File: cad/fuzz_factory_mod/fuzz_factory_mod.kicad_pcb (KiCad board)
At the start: 2 copper layers, 138 x 114 mm, 390 parts, among them J101 Conn_interface_1, J102 Conn_interface_2, J1701 Barrel_Jack_Switch, J1702 Conn_Battery, J1703 CONN_AUDIO_IN, J1704 CONN_AUDIO_OUT, J201 Conn_MCU_SWD, J2801 CONN_AUDIO_OUT_REF, J2802 CONN_EXP_1, J2803 CONN_EXP_2, J301 USB_B_Micro, J401 USB_B_Micro, J901 CONN_MIDI_IN, J902 CONN_MIDI_THRU, J903 CONN_MIDI_OUT, J904 Conn_01x10_Female, J905 Conn_01x10_Female, K2101 Fujitsu-Takamisawa-A_AL, Q1301 MMDT3904, Q1302 MMDT3904, Q1602 DTA123Y, Q1603 DTA123Y, Q1604 DTA123Y, Q1605 DTA123Y, Q1701 DTC114Y, Q1702 DTA114E, Q2201 BCP51, Q601 DTA123Y, Q602 DTA123Y, Q603 DTA123Y, Q604 DTA123Y, Q801 MMDT3904, Q802 MMDT3904, SW1101 SW_PUSH, SW1201 SW_PUSH, SW1301 SW_PUSH, U1101 LM1458, U1102 MC33202, U1201 LM2903, U1202 MC33202, U1501 LM1458, U1502 MC33202, U1503 MC33202, U1601 4050, U1602 4049, U1603 4504, U1604 MC33202, U1701 LM1458, U1702 MC33202, U1803 LM1458, U1804 MC33202, U1901 LM2903, U201 STM32F303VCTx, U2201 TL072, U2202 LM2674M-ADJ, U2203 LM78L05_SO8, U301 USBLC6-2SC6, U302 FT230XS, U401 USBLC6-2SC6, U501 74LS132, U601 4050, U602 4504, U603 MC33202, U604 4049, U701 AD5262_ABC, U901 4N25, Y201 Resonator_Small

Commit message: Continued layout.
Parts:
- moved C2211 304.2 mm to (234.6, 109.4), turned to 0 degrees
- moved C2202 284.5 mm to (225.7, 109.4)
- moved C2206 277.4 mm to (225.7, 116.0), turned to 0 degrees
- moved R1702 273.0 mm to (102.2, 49.8)
- moved C210 270.5 mm to (139.8, 90.8), turned to 0 degrees
- moved R207 267.4 mm to (136.8, 90.8), turned to 0 degrees
- moved R1505 262.2 mm to (97.8, 106.2), turned to 270 degrees
- moved D1701 257.7 mm to (79.8, 42.0)
- moved R808 254.7 mm to (104.8, 64.2), turned to 0 degrees
- moved Q1701 254.5 mm to (80.8, 46.8), turned to 180 degrees
- moved R815 254.4 mm to (104.8, 65.9), turned to 0 degrees
- moved R807 254.2 mm to (104.8, 67.7), turned to 0 degrees
- moved K2101 253.6 mm to (69.5, 46.8), turned to 0 degrees
- moved R1510 253.4 mm to (92.2, 125.5), turned to 90 degrees
- moved R1306 253.4 mm to (129.5, 104.5), turned to 0 degrees
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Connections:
- C907 pad 2: +5V -> /MCU/MIDI/+5V_IN
- R205 pad 1: +5V -> /MCU/MIDI/+5V_IN
- R206 pad 1: +5V -> /MCU/MIDI/+5V_IN
- R918 pad 2: +5V -> /MCU/MIDI/+5V_IN
- R920 pad 1: +5V -> /MCU/MIDI/+5V_IN
- R922 pad 1: +5V -> /MCU/MIDI/+5V_IN
- U501 pad 14: +5V -> /MCU/MIDI/+5V_IN
- U901 pad 6: +5V -> /MCU/MIDI/+5V_IN
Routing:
- net +3V3: track 88.2 -> 4.71 mm, vias 2 -> 0
- net BYPASS_CMD: track 0.00 -> 82.0 mm, vias 0 -> 4
- net DISP_ENABLE: track 0.00 -> 80.5 mm, vias 0 -> 2
- net SPI2_MOSI: track 0.00 -> 77.3 mm, vias 0 -> 2
- net SPI2_SCK: track 0.00 -> 76.5 mm, vias 0 -> 2
- net /CONNECTORS/AUDIO_IN_CONN: track 0.00 -> 67.2 mm
- net GNDD: track 16.9 -> 59.5 mm, vias 5 -> 16
- net ENC3_IN_CW: track 0.00 -> 34.8 mm
- net ENC3_IN_CCW: track 0.00 -> 34.7 mm
- net ENC1_IN_CCW: track 0.00 -> 34.6 mm, vias 0 -> 2
- net /CONNECTORS/AUDIO_OUT_CONN: track 0.00 -> 34.0 mm
- net DISP_LATCH: track 0.00 -> 33.3 mm, vias 0 -> 2
- net +9V: track 22.9 -> 54.0 mm
- net ENC1__LED_GREEN: track 0.00 -> 30.0 mm, vias 0 -> 2
- net ENC1_IN_CW: track 0.00 -> 28.7 mm, vias 0 -> 2
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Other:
- board text added: "0.5mm clearance with enclosure wall"

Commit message: Continued layout.
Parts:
- C1112, C701: moved to F.Cu
- moved C2211 56.5 mm to (180.8, 92.5), turned to 180 degrees
- moved C1110 56.0 mm to (135.8, 89.6)
- moved R207 48.3 mm to (166.5, 52.8), turned to 270 degrees
- moved R208 48.0 mm to (168.8, 52.8), turned to 270 degrees
- moved C2202 46.2 mm to (180.8, 98.5), turned to 180 degrees
- moved C210 44.1 mm to (166.5, 55.8), turned to 270 degrees
- moved C211 43.7 mm to (168.8, 55.8), turned to 270 degrees
- moved Q1702 36.7 mm to (171.2, 90.2)
- moved C2206 33.5 mm to (199.5, 95.0), turned to 270 degrees
- moved R2804 22.5 mm to (187.5, 49.5)
- moved R2802 19.3 mm to (166.5, 50.0)
- moved C1304 16.7 mm to (184.2, 125.0)
- moved R505 16.4 mm to (140.2, 96.5), turned to 0 degrees
- moved R804 16.3 mm to (94.8, 64.2), turned to 0 degrees
- moved R502 14.0 mm to (140.2, 98.2), turned to 0 degrees
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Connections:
- net Net-(C2207-Pad2) renamed /PSU/DCDC_VSW
- J102 pad 5: ENC2_IN_CCW -> ENC2_IN_CW
- U201 pad 82: ENC2_IN_CCW -> ENC2_IN_CW
- U201 pad 92: ENC2_IN_CCW -> (no net)
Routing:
- net AUDIO_OUT_FX: track 0.00 -> 182.0 mm, vias 0 -> 7
- net AUDIO_IN_FX: track 0.00 -> 134.1 mm, vias 0 -> 4
- net /MCU/SW_PRESET_UP: track 0.00 -> 119.3 mm, vias 0 -> 2
- net /MCU/UART5_RX: track 1.27 -> 115.8 mm, vias 0 -> 2
- net /MCU/SW_PRESET_DOWN: track 8.50 -> 116.8 mm, vias 0 -> 2
- net USB_DP: track 0.00 -> 100.6 mm, vias 0 -> 2
- net USB_DM: track 0.00 -> 100.1 mm, vias 0 -> 2
- net INPUT_CAPTURE_2: track 2.54 -> 96.7 mm, vias 0 -> 2
- net INPUT_CAPTURE_1: track 4.76 -> 93.8 mm, vias 0 -> 2
- net /ANALOG/IN_AUDIO_VCA: track 4.12 -> 84.0 mm, vias 0 -> 3
- net Net-(C2201-Pad1): track 0.00 -> 75.4 mm
- net /MCU/SW_BYPASS: track 2.30 -> 76.0 mm, vias 1 -> 5
- net Ref_Stab_DAC_PWM_MSB: track 13.2 -> 84.6 mm, vias 1 -> 4
- net Ref_Stab_DAC_PWM_LSB: track 6.32 -> 76.0 mm, vias 1 -> 5
- net VCA_IN_PWM: track 0.00 -> 68.7 mm, vias 0 -> 2
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- added copper zone on F.Cu, net +3V3
- added copper zone on F.Cu, net /PSU/DCDC_VSW

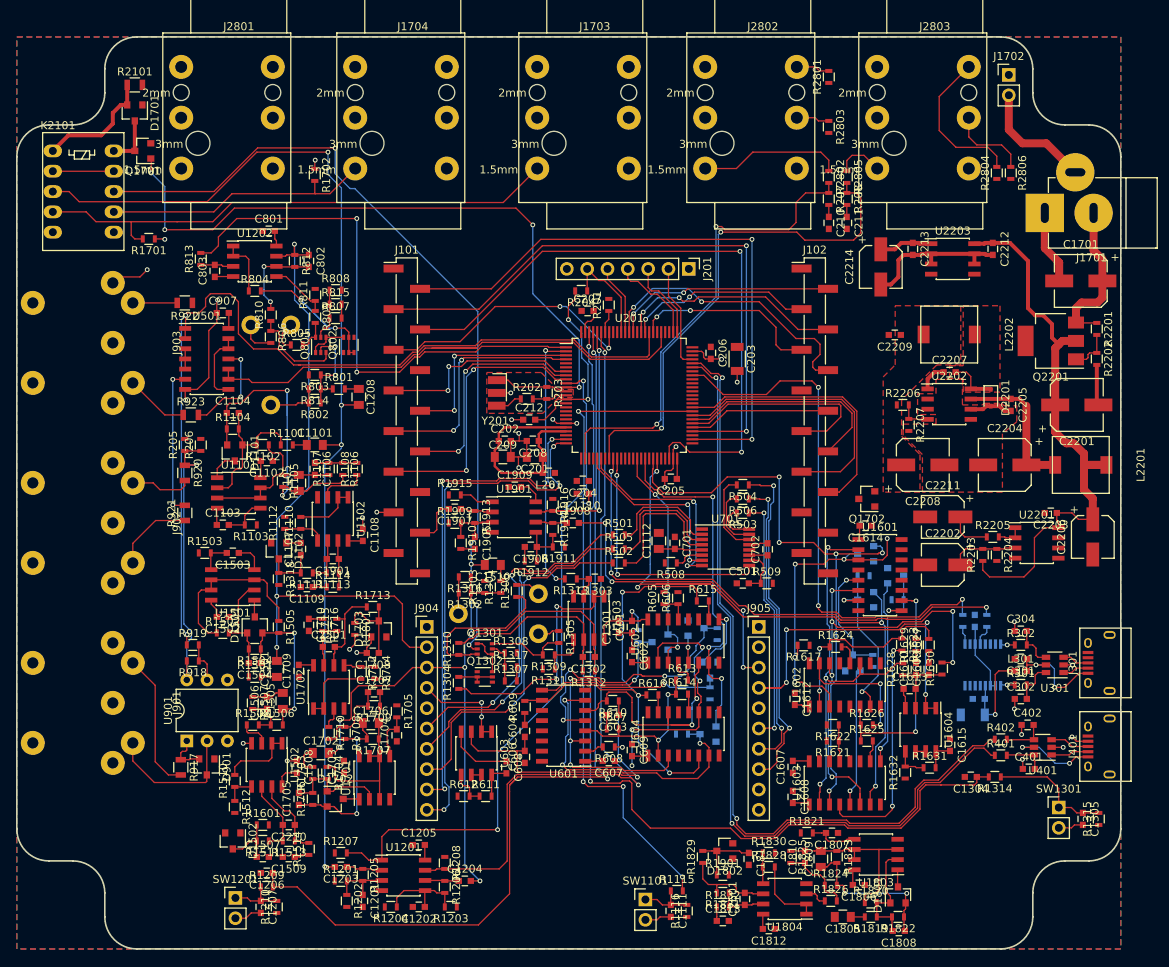
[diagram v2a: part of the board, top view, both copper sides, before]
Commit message: Continued layout. Started power planes.
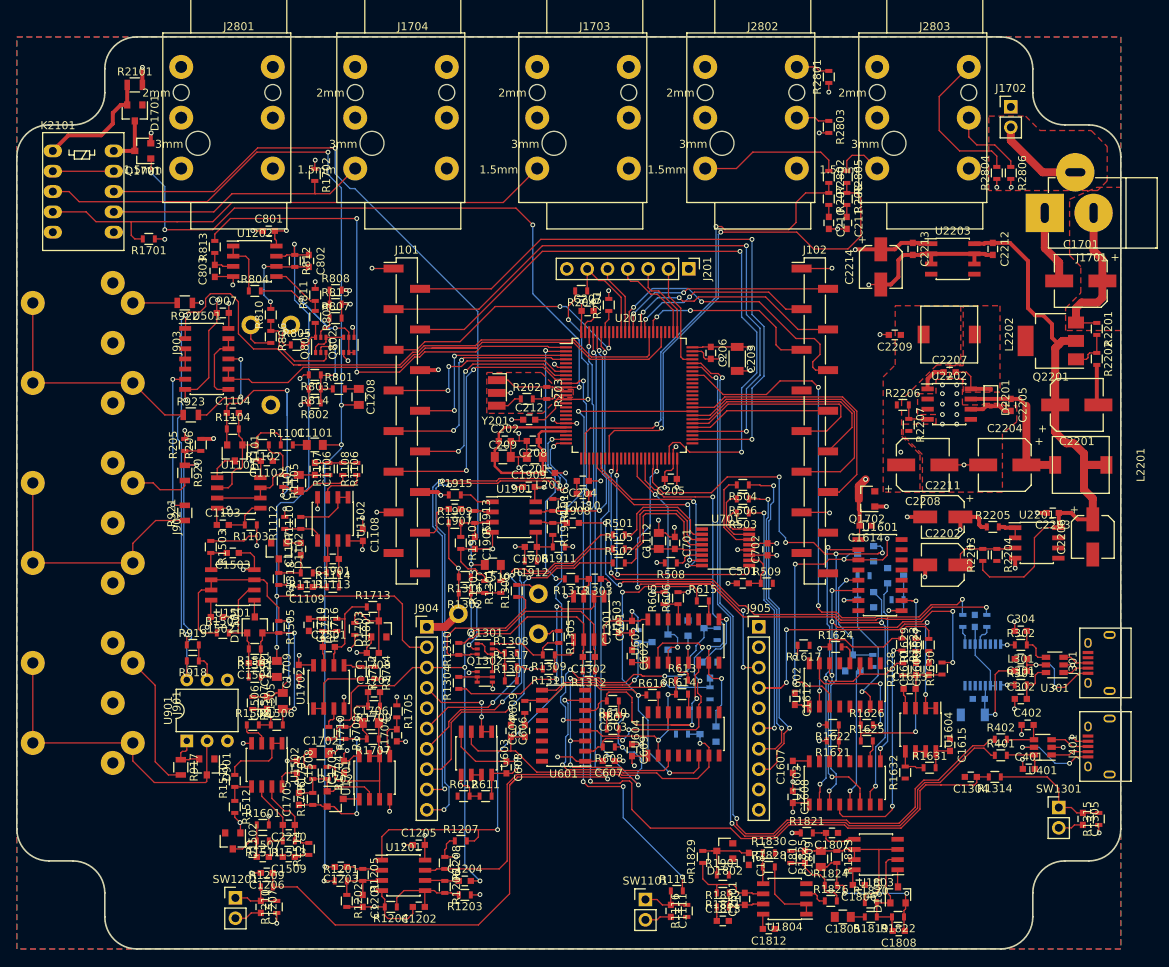
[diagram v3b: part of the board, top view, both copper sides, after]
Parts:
- moved R1207 15.1 mm to (120.5, 133.0)
- moved J1702 4.01 mm to (189.2, 41.2)
- moved C606 3.69 mm to (126.8, 119.2), turned to 270 degrees
- moved R1203 2.30 mm to (121.0, 139.8)
- moved R813 2.30 mm to (89.8, 58.8)
- moved C1909 1.75 mm to (129.0, 88.8)
- moved R2205 1.25 mm to (187.0, 93.8)
- moved R1503 1.06 mm to (89.2, 96.2), turned to 270 degrees
- moved C1502 0.75 mm to (90.0, 105.0)
- moved C2203 0.25 mm to (194.5, 92.0)
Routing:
- net +3V3: track 9.09 -> 612.9 mm, vias 0 -> 20
- net +9V: track 74.6 -> 559.0 mm, vias 2 -> 26
- net VCOM: track 5.48 -> 189.3 mm, vias 0 -> 4
- net +BATT: track 19.3 -> 161.9 mm, vias 0 -> 1
- net +5V: track 6.67 -> 117.2 mm, vias 0 -> 3
- net GNDA: track 52.5 -> 131.2 mm, vias 11 -> 53
- net /MCU/MIDI/+5V_IN: track 38.6 -> 76.8 mm, vias 1 -> 3
- net GNDD: track 92.0 -> 115.8 mm, vias 17 -> 39
- net Net-(J902-Pad5): track 10.1 -> 32.6 mm
- net Net-(J903-Pad5): track 7.96 -> 30.5 mm
- net Net-(D901-Pad3): track 17.9 -> 40.4 mm
- net Net-(C1505-Pad2): track 26.1 -> 37.0 mm, vias 0 -> 2
- net Net-(J1701-Pad3): track 14.8 -> 11.4 mm
- net ADC_FF_pol2: track 65.4 -> 68.3 mm
- net ADC_FF_pol1: track 63.1 -> 65.7 mm
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- added copper zone on In2.Cu, net +3V3
- added copper zone on F.Cu, net +BATT
- added copper zone on In2.Cu, net +BATT
- added copper zone on In1.Cu, net GNDA
- added copper zone on In2.Cu, net GNDA
- added copper zone on F.Cu, net Net-(J1701-Pad3)
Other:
- copper layers 2 -> 4

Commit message: Layout continued : finished power polys on internal layer.
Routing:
- net +3V3: track 612.9 -> 610.2 mm
- net VCOM: track 189.3 -> 187.1 mm
- net /MCU/MIDI/+5V_IN: track 76.8 -> 77.7 mm
- added copper zone on In2.Cu, net +5V
- added copper zone on In2.Cu, net +9V
- added copper zone on In2.Cu, net VCOM

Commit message: Continued layout.
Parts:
- removed NT101, NT102: Net-Tie_2, Oddities:NetTie-II
- moved R2801 8.31 mm to (168.8, 45.5)
- moved R2803 1.75 mm to (166.5, 45.5)
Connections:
- C1110 pad 2: GNDD -> GNDA
- C1111 pad 2: GNDD -> GNDA
- C1206 pad 2: GNDD -> GNDA
- C1207 pad 2: GNDD -> GNDA
- C1304 pad 2: GNDD -> GNDA
- C1305 pad 2: GNDD -> GNDA
- C1701 pad 2: GNDPWR -> GNDA
- C203 pad 2: GNDD -> GNDA
- C204 pad 2: GNDD -> GNDA
- C205 pad 2: GNDD -> GNDA
- C206 pad 2: GNDD -> GNDA
- C207 pad 2: GNDD -> GNDA
- C210 pad 2: GNDD -> GNDA
- C211 pad 2: GNDD -> GNDA
- C212 pad 1: GNDD -> GNDA
- C2201 pad 2: GNDD -> GNDA
- C2204 pad 2: GNDD -> GNDA
- C2205 pad 2: GNDD -> GNDA
- C2206 pad 2: GNDD -> GNDA
- C2208 pad 2: GNDD -> GNDA
- C2209 pad 2: GNDD -> GNDA
- C2212 pad 2: GNDD -> GNDA
- C2213 pad 2: GNDD -> GNDA
- C2214 pad 2: GNDD -> GNDA
- C301 pad 2: GNDD -> GNDA
- C302 pad 1: GNDD -> GNDA
- C303 pad 2: GNDD -> GNDA
- C304 pad 1: GNDD -> GNDA
- C305 pad 2: GNDD -> GNDA
- C306 pad 1: GNDD -> GNDA
- C401 pad 1: GNDD -> GNDA
- C402 pad 1: GNDD -> GNDA
- C702 pad 1: GNDD -> GNDA
- C907 pad 1: GNDD -> GNDA
- D2201 pad 2: GNDD -> GNDA
- J101 pad 1: GNDD -> GNDA
- J101 pad 13: GNDD -> GNDA
- J102 pad 1: GNDD -> GNDA
- J102 pad 13: GNDD -> GNDA
- J1701 pad 1: GNDPWR -> GNDA
- J1702 pad 1: GNDS -> Net-(J1702-Pad1)
- J1703 pad 1: GNDPWR -> GNDA
- J1703 pad 4: GNDPWR -> GNDA
- J1703 pad 5: (no net) -> Net-(J1702-Pad1)
- J1704 pad 1: GNDPWR -> GNDA
- J1704 pad 4: GNDPWR -> GNDA
- J1704 pad 5: GNDS -> (no net)
- J201 pad 7: GNDD -> GNDA
- J2801 pad 1: GNDPWR -> GNDA
- J2801 pad 4: GNDPWR -> GNDA
- J2802 pad 1: GNDD -> GNDA
- J2802 pad 6: GNDD -> GNDA
- J2803 pad 1: GNDD -> GNDA
- J2803 pad 6: GNDD -> GNDA
- J301 pad 4: GNDD -> GNDA
- J301 pad 5: GNDD -> GNDA
- J301 pad 6: GNDD -> GNDA
- J401 pad 4: GNDD -> GNDA
- J401 pad 5: GNDD -> GNDA
- J401 pad 6: GNDD -> GNDA
- J902 pad 2: GNDD -> GNDA
- J903 pad 2: GNDD -> GNDA
- Q1701 pad 2: GNDPWR -> GNDA
- R201 pad 2: GNDD -> GNDA
- R2202 pad 2: GNDD -> GNDA
- R2207 pad 2: GNDD -> GNDA
- R2803 pad 2: GNDD -> GNDA
- R2806 pad 2: GNDD -> GNDA
- SW1101 pad 2: GNDD -> GNDA
- SW1201 pad 2: GNDD -> GNDA
- SW1301 pad 2: GNDD -> GNDA
- U201 pad 49: GNDD -> GNDA
- U201 pad 74: GNDD -> GNDA
- U201 pad 99: GNDD -> GNDA
- U2202 pad 6: GNDD -> GNDA
- U2203 pad 2: GNDD -> GNDA
- U2203 pad 3: GNDD -> GNDA
- U2203 pad 6: GNDD -> GNDA
- U2203 pad 7: GNDD -> GNDA
- U301 pad 2: GNDD -> GNDA
- U302 pad 13: GNDD -> GNDA
- U302 pad 5: GNDD -> GNDA
- U401 pad 2: GNDD -> GNDA
- U501 pad 7: GNDD -> GNDA
- U701 pad 11: GNDD -> GNDA
- U901 pad 4: GNDD -> GNDA
- Y201 pad 2: GNDD -> GNDA
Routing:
- net GNDA: track 131.2 -> 270.8 mm, vias 53 -> 99
- net GNDD: track 115.8 -> 0.00 mm, vias 39 -> 0
- net +9V: track 559.0 -> 644.3 mm, vias 26 -> 34
- net Net-(J1702-Pad1): track 0.00 -> 68.8 mm
- net AUDIO_OUT_FX: track 182.0 -> 240.0 mm, vias 7 -> 11
- net +3V3: track 610.2 -> 626.4 mm, vias 20 -> 25
- net GNDPWR: track 10.6 -> 0.00 mm, vias 1 -> 0
- net Net-(J2802-Pad4): track 4.21 -> 13.9 mm
- net +BATT: track 161.9 -> 158.3 mm
- net /MCU/SW_BYPASS: track 76.0 -> 79.2 mm
- net VCOM: track 187.1 -> 189.4 mm
- net Net-(J2803-Pad4): track 19.4 -> 17.3 mm
- net Net-(J2802-Pad3): track 18.1 -> 19.8 mm
- net FF_Stab_DAC_PWM_MSB: track 44.4 -> 46.0 mm
- net Net-(C1808-Pad1): track 19.5 -> 21.2 mm
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- removed copper zone on F.Cu, net GNDD

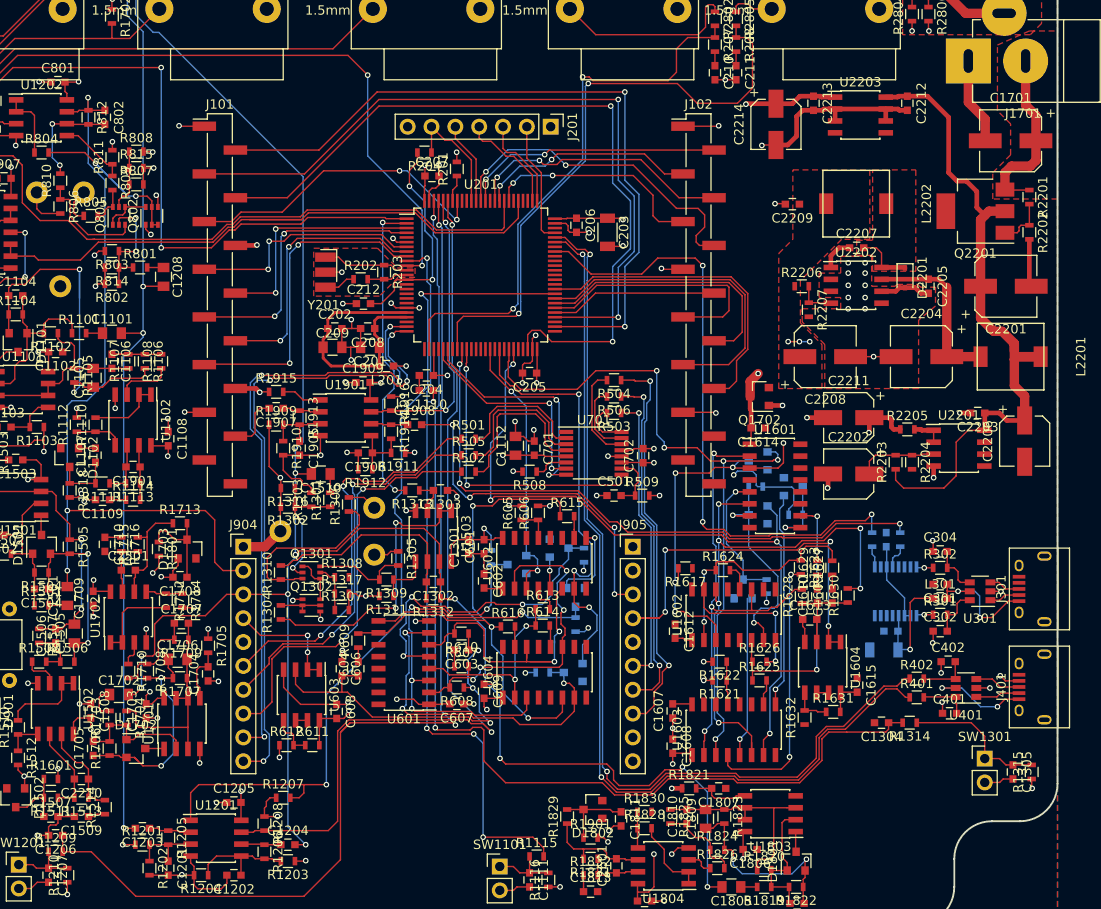
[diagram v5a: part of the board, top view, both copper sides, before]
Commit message: Layout finished : 0 unrouted, to be cleaned.
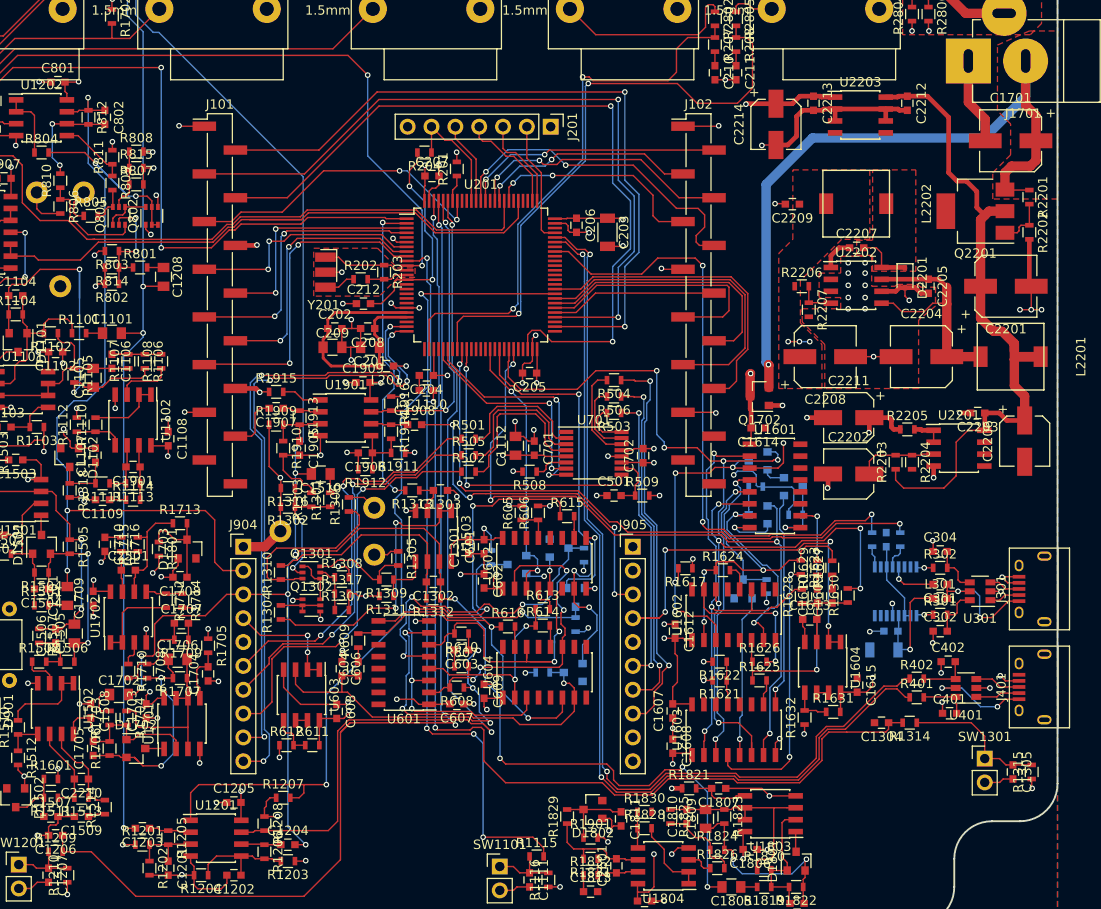
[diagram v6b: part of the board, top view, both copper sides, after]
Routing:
- net GNDA: track 270.8 -> 328.3 mm, vias 99 -> 120
- net +BATT: track 158.3 -> 215.4 mm, vias 1 -> 2
- net +9V: track 644.3 -> 670.6 mm, vias 34 -> 37
- net /ANALOG/DAC_REF/IN_PWM_LSBn_BUFF: track 25.1 -> 38.7 mm, vias 2 -> 4
- net Net-(C2204-Pad1): track 18.3 -> 26.0 mm
- net +3V3: track 626.4 -> 632.3 mm, vias 25 -> 26
- net Net-(Q601-Pad3): track 42.3 -> 44.2 mm
- net /ANALOG/IN_AUDIO_VCA: track 85.0 -> 85.8 mm
- net Net-(Q1604-Pad3): track 25.1 -> 25.8 mm
- net Net-(Q602-Pad3): track 33.8 -> 34.4 mm
- net /ANALOG/DAC_REF/IN_PWM_MSB_BUFF: track 60.1 -> 60.6 mm
- net /ANALOG/DAC_REF/IN_PWM_LSB_BUFF: track 49.9 -> 50.5 mm
- net Net-(Q1301-Pad6): track 10.0 -> 10.6 mm

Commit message: Continued layout.
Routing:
- net /MCU/SW_PRESET_DOWN: track 116.8 -> 92.7 mm
- net +3V3: track 632.3 -> 626.1 mm
- net DISP_LATCH: track 33.3 -> 37.5 mm
- net SPI_FF_Gain_SCK: track 23.0 -> 26.1 mm
- net /MCU/UART5_TX: track 66.5 -> 63.5 mm
- net AUDIO_OUT_FX: track 240.0 -> 242.3 mm
- net ENC2_IN_CCW: track 35.8 -> 38.1 mm
- net /ANALOG/GAIN_POT_REF_3: track 42.3 -> 44.5 mm
- net INPUT_CAPTURE_2: track 97.1 -> 99.3 mm
- net /MCU/UART5_RX: track 116.1 -> 118.2 mm
- net VCA_OUT_PWM: track 33.7 -> 35.9 mm
- net INPUT_CAPTURE_3: track 33.6 -> 31.8 mm
- net /ANALOG/GAIN_POT_REF_2: track 36.9 -> 38.6 mm
- net VCA_IN_PWM: track 66.1 -> 67.8 mm
- net ADC_FF_pol2: track 68.3 -> 66.7 mm
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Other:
- net class Default: clearance 0.15 -> 0.175; trace_width 0.15 -> 0.175; via_dia 0.6 -> 0.9
- rule trace_clearance: 0.15 -> 0.175
- rule trace_min: 0.15 -> 0.175
- rule via_min_size: 0.6 -> 0.9
